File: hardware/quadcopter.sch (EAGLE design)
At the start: 61 parts, among them J1 AVR_SPI_PRG_6NS, J2 HEADER-4POS-2X2-0.1IN-FEMALE-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, J3 HEADER-10POSTH-254X10, J4 HEADER-4POS-0.1IN-FEMALE-SMD-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, Q1 MOSFET-SI2302CDS-T1-E3CT-ND, Q2 MOSFET-SI2302CDS-T1-E3CT-ND, Q3 MOSFET-SI2302CDS-T1-E3CT-ND, Q4 MOSFET-SI2302CDS-T1-E3CT-ND, Q5 MOSFET-SI2302CDS-T1-E3CT-ND, Q6 MOSFET-SI2302CDS-T1-E3CT-ND, SW1 PUSHBUTTON_SMD-VERTICAL-1, U1 ATMEGA128RFA1, U2 LSM-IMU-497-18367-1-NDIMU, Y1 CRYSTAL5X3

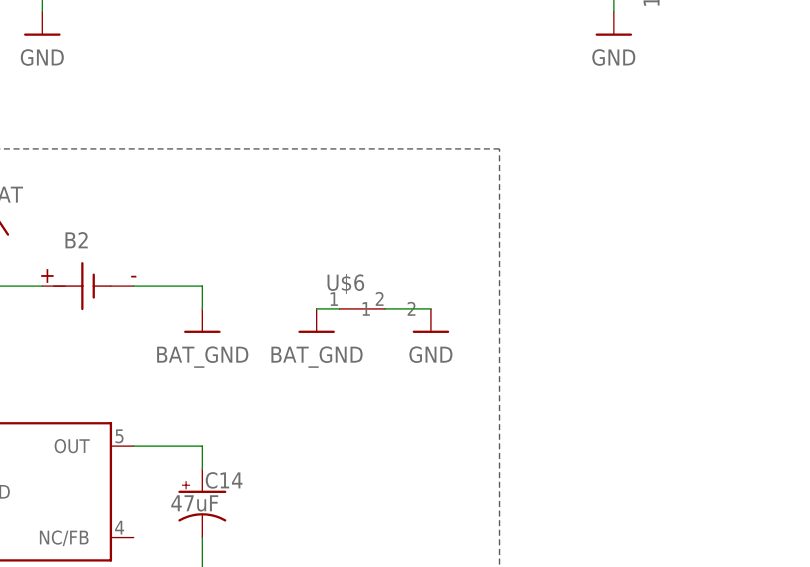
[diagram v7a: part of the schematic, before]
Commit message: renamed net bridge
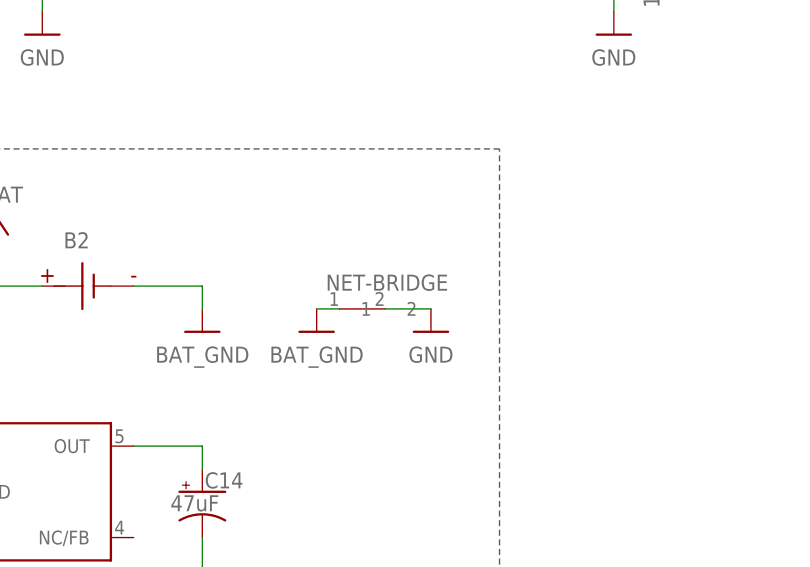
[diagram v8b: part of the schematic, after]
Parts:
- renumbered U$6 to NET-BRIDGE
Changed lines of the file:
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@@
 <part name="GND34" library="quadparts_prebuilt_2022" deviceset="BAT_GND" device=""/>
 <part name="P+14" library="quadparts_prebuilt_2022" deviceset="VBAT" device=""/>
-<part name="U$6" library="custom.lbr" library_urn="urn:adsk.wipprod:fs.file:vf.FjMADskDQ2Se9fX1PD5xcw" deviceset="NET-BRIDGE" device=""/>
+<part name="NET-BRIDGE" library="custom.lbr" library_urn="urn:adsk.wipprod:fs.file:vf.FjMADskDQ2Se9fX1PD5xcw" deviceset="NET-BRIDGE" device=""/>
 <part name="GND37" library="quadparts_prebuilt_2022" deviceset="BAT_GND" device=""/>
 <part name="GND38" library="quadparts_prebuilt_2022" deviceset="GND" device=""/>
@@
 <attribute name="VALUE" x="233.68" y="50.8" size="1.778" layer="96" rot="R180" align="center"/>
 </instance>
-<instance part="U$6" gate="G$1" x="274.32" y="38.1" smashed="yes">
+<instance part="NET-BRIDGE" gate="G$1" x="274.32" y="38.1" smashed="yes">
 <attribute name="NAME" x="270.256" y="40.132" size="1.778" layer="95"/>
 </instance>
@@
 <wire x1="276.86" y1="38.1" x2="281.94" y2="38.1" width="0.1524" layer="91"/>
 <pinref part="GND38" gate="1" pin="GND"/>
-<pinref part="U$6" gate="G$1" pin="2"/>
+<pinref part="NET-BRIDGE" gate="G$1" pin="2"/>
 </segment>
 <segment>
@@
 <pinref part="GND37" gate="1" pin="BAT_GND"/>
 <wire x1="269.24" y1="38.1" x2="271.78" y2="38.1" width="0.1524" layer="91"/>
-<pinref part="U$6" gate="G$1" pin="1"/>
-</segment>
-<segment>
+<pinref part="NET-BRIDGE" gate="G$1" pin="1"/>
+</segment>
+<segment>
